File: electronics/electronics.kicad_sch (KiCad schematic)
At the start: 0 parts

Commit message: 6 stepper wiring
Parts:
- added A1: RaspberryPi_Pico, Module:RaspberryPi_Pico_Common_Unspecified, symbol MCU_Module:RaspberryPi_Pico
- added BT1: Battery, symbol Device:Battery
- added M1, M2, M3, M4, M5, M6: Stepper_Motor_bipolar, symbol Motor:Stepper_Motor_bipolar
- added U1: L7805, symbol Regulator_Linear:L7805
- added U2, U3, U4, U5, U6, U7: ULN2003, symbol Transistor_Array:ULN2003
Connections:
- new net: A1.17 (GPIO13), U5.1 (I1)
- new net: M4.4, U5.13 (O4)
- new net: M4.3, U5.14 (O3)
- new net: M4.2 (-), U5.15 (O2)
- new net: M4.1, U5.16 (O1)
- new net: A1.16 (GPIO12), U5.2 (I2)
- new net: A1.15 (GPIO11), U5.3 (I3)
- new net: A1.14 (GPIO10), U5.4 (I4)
- new net: A1.39 (VSYS), U1.3 (OUT), U2.9 (COM), U3.9 (COM), U4.9 (COM), U5.9 (COM), U6.9 (COM), U7.9 (COM)
- new net: A1.26 (GPIO20), U2.1 (I1)
- new net: M1.4, U2.13 (O4)
- new net: M1.3, U2.14 (O3)
- new net: M1.2 (-), U2.15 (O2)
- new net: M1.1, U2.16 (O1)
- new net: A1.27 (GPIO21), U2.2 (I2)
- new net: A1.29 (GPIO22), U2.3 (I3)
- new net: A1.31 (GPIO26_ADC0), U2.4 (I4)
- new net: A1.13 (GND), A1.18 (GND), A1.23 (GND), A1.28 (GND), A1.3 (GND), A1.38 (GND), A1.8 (GND), BT1.2 (-), U2.8 (GND), U3.8 (GND), U4.8 (GND)
- new net: M3.1, U4.16 (O1)
- new net: M3.2 (-), U4.15 (O2)
- new net: M3.3, U4.14 (O3)
- new net: M3.4, U4.13 (O4)
- new net: M2.1, U3.16 (O1)
- new net: M2.2 (-), U3.15 (O2)
- new net: M2.3, U3.14 (O3)
- new net: M2.4, U3.13 (O4)
- new net: A1.10 (GPIO7), U6.3 (I3)
- new net: A1.11 (GPIO8), U6.2 (I2)
- new net: A1.12 (GPIO9), U6.1 (I1)
- new net: A1.19 (GPIO14), U3.4 (I4)
- new net: A1.20 (GPIO15), U3.3 (I3)
- new net: A1.21 (GPIO16), U4.1 (I1)
- new net: A1.22 (GPIO17), U4.2 (I2)
- new net: A1.24 (GPIO18), U4.3 (I3)
- new net: A1.25 (GPIO19), U4.4 (I4)
- new net: A1.32 (GPIO27_ADC1), U3.1 (I1)
- new net: A1.34 (GPIO28_ADC2), U3.2 (I2)
- new net: A1.4 (GPIO2), U7.4 (I4)
- new net: A1.5 (GPIO3), U7.3 (I3)
- new net: A1.6 (GPIO4), U7.2 (I2)
- new net: A1.7 (GPIO5), U7.1 (I1)
- new net: A1.9 (GPIO6), U6.4 (I4)
- new net: M6.4, U7.13 (O4)
- new net: M6.3, U7.14 (O3)
- new net: M6.2 (-), U7.15 (O2)
- new net: M6.1, U7.16 (O1)
- new net: BT1.1 (+), U1.1 (IN)
- new net: M5.4, U6.13 (O4)
- new net: M5.3, U6.14 (O3)
- new net: M5.2 (-), U6.15 (O2)
- new net: M5.1, U6.16 (O1)
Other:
- note added: "5V"
- note added: "GND"
- note added: "VCC"

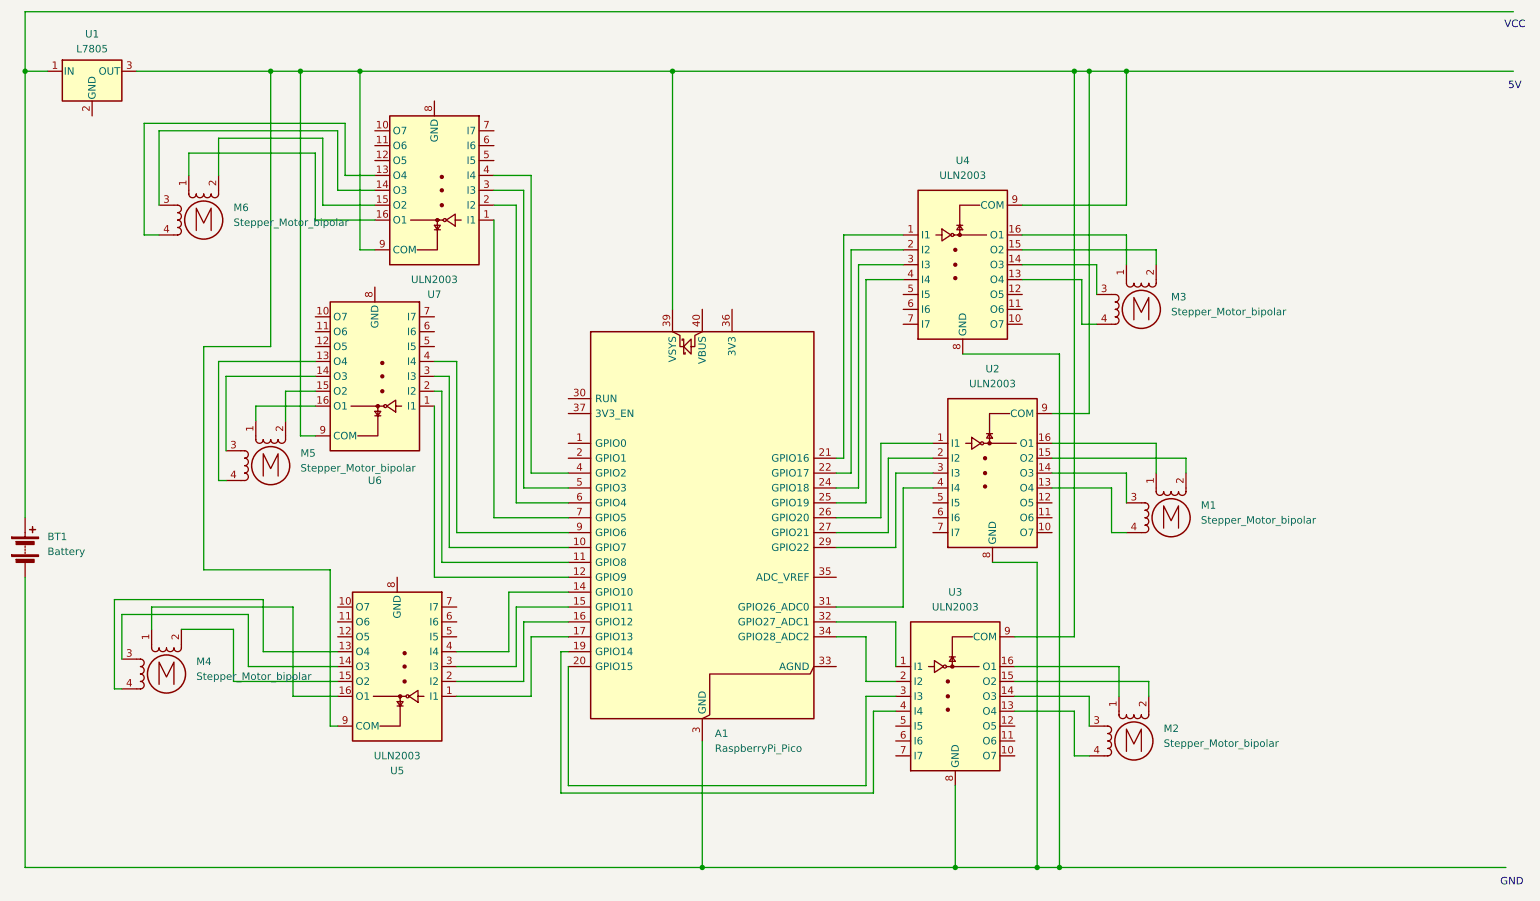
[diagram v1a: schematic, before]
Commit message: c++ stuff, basic stepper commands done
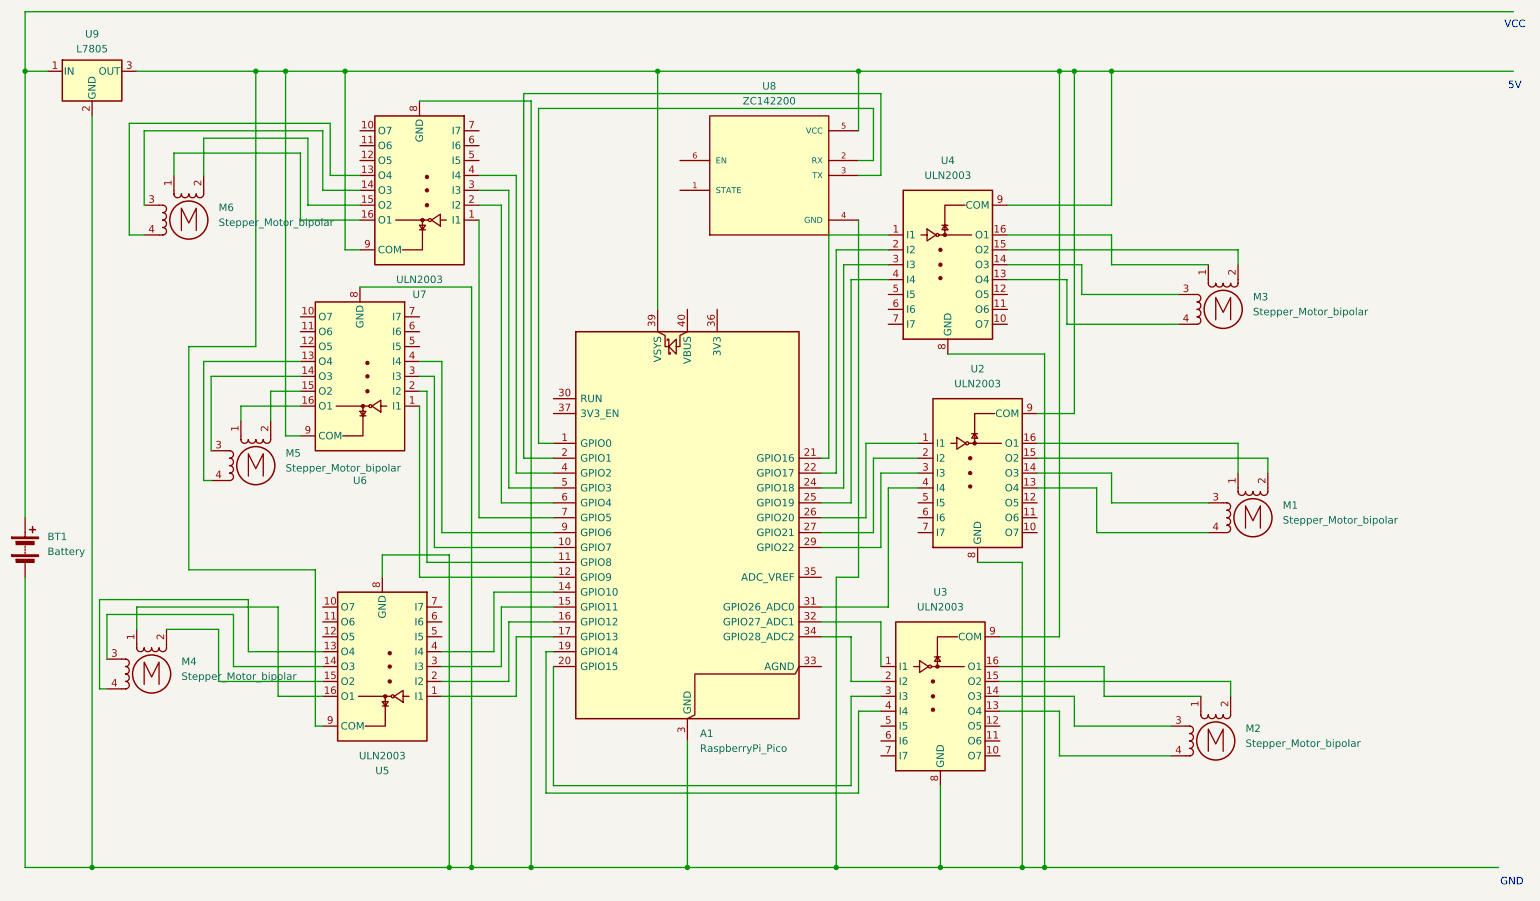
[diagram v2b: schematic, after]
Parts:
- removed U1: L7805, symbol Regulator_Linear:L7805
- added U8: ZC142200, ZC142200:MODULE_ZC142200, symbol ZC142200:ZC142200
- added U9: L7805, symbol Regulator_Linear:L7805
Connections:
- net at U5.8 (GND): now also A1.13 (GND), A1.18 (GND), A1.23 (GND), A1.28 (GND), A1.3 (GND), A1.38 (GND), A1.8 (GND), BT1.2 (-), U2.8 (GND), U3.8 (GND), U4.8 (GND), U6.8 (GND), U7.8 (GND), U8.4 (GND), U9.2 (GND)
- net at A1.39 (VSYS), U2.9 (COM), U3.9 (COM)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: now also U8.5 (VCC), U9.3 (OUT)
- net at A1.1 (GPIO0): now also U8.2 (RX)
- net at A1.2 (GPIO1): now also U8.3 (TX)
- net at BT1.1 (+): now also U9.1 (IN)
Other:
- moved on the sheet: A1, M1, M2, M3, M4, M5, M6, U2, U3, U4, U5, U6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
